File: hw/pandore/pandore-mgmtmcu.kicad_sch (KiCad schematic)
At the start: 40 parts, among them J17 GROVE, J18 GROVE, J25 DISPLAY, J26 RGBA, Q10 MOSFET_EN-N, Q8 MOSFET_EN-N, Q9 MOSFET_EN-N, U25 x4xxxx1G04

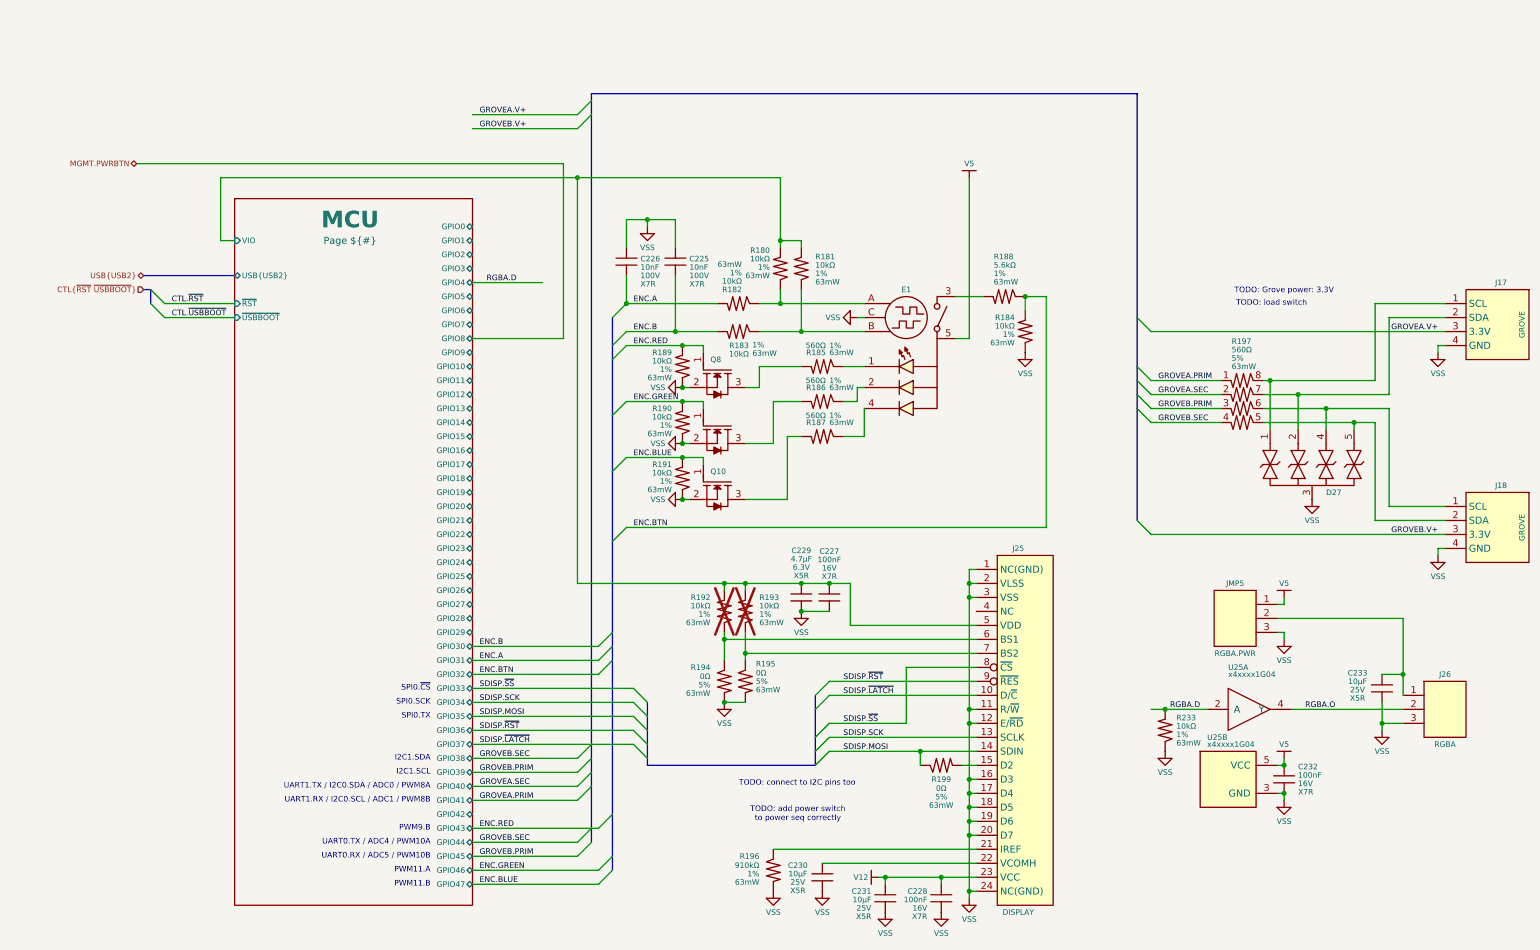
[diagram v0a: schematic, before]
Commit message: added expansion port and more ctl to rp2350s routing much progress
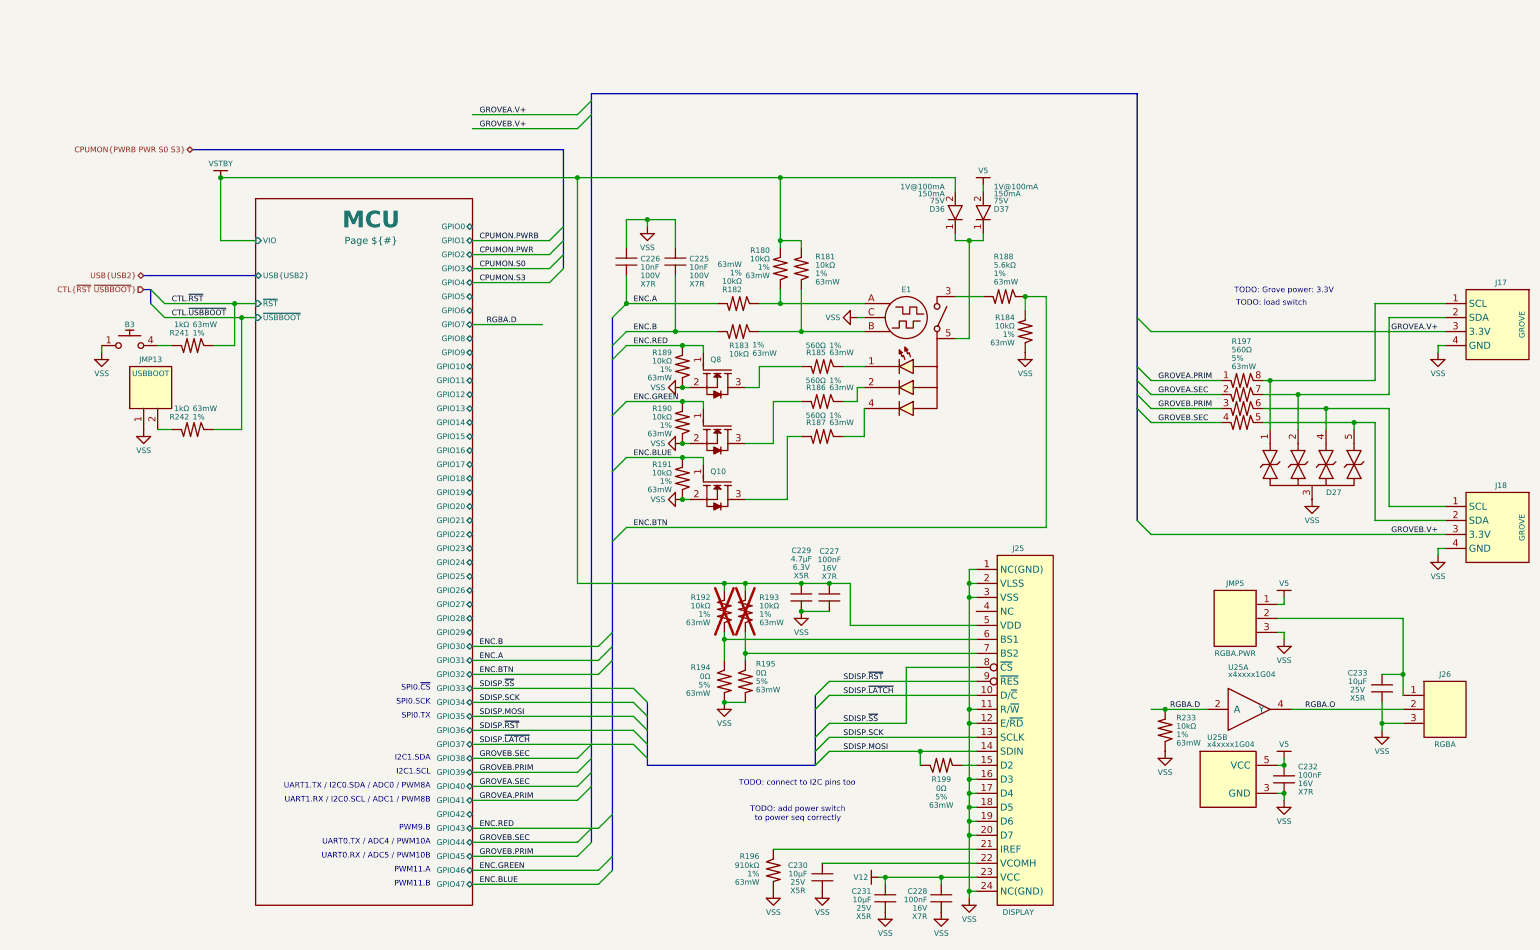
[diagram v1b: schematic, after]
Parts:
- added B3: mom_tact_no, reekilib_msw:tact_460X320X250, symbol reekilib_msw:mom_tact_no
- added D36, D37: ${Vr}, ${Io}, ${Vf}, reekilib_sod:sod-123, symbol reekilib_dio:diode
- added JMP13: USBBOOT, reekilib_con:HDR254P1X02-TH, symbol reekilib_con:hdr-1x2
- added R241, R242: ${Resistance}, ${Tolerance}, ${Power}, reekilib_res:RESC1005, symbol reekilib_res:res
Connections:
- net CTL.~{RST}: now also R241.2
- net CTL.~{USBBOOT}: now also R242.2
- net V5: now also D37.2 (A); no longer E1.5 (CM)
- net VSS: now also B3.1, B3.2, JMP13.1
- net MCU/VIO renamed VSTBY
- net VSTBY: now also D36.2 (A)
- new net: D36.1 (C), D37.1 (C), E1.5 (CM)
- new net: JMP13.2, R242.1
- new net: B3.3, B3.4, R241.1

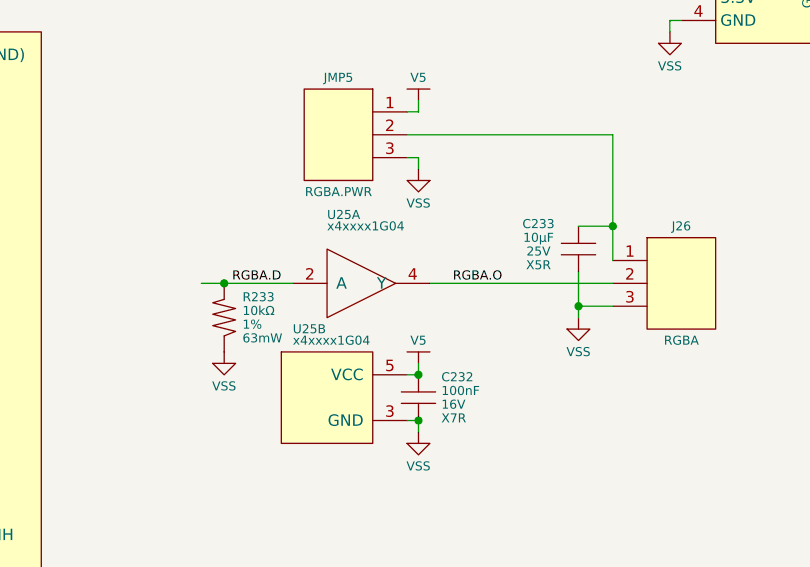
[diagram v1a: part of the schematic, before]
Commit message: more routing/placement done added 5v load switch 1A each added second fan circuit redone all diffpair routing following new stackup calc added all (?) missing connectors to unused pins
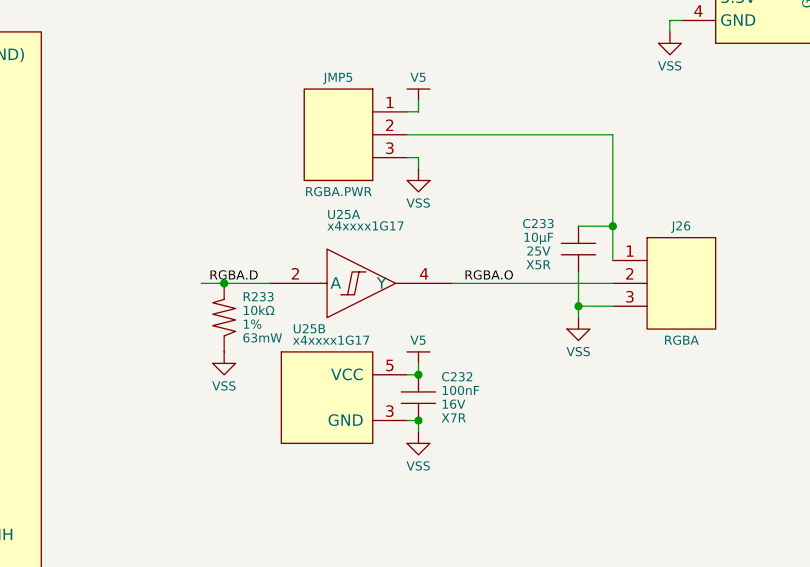
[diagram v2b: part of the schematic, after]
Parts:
- removed U25: x4xxxx1G04, reekilib_sot:SOT65P210X90-5, symbol reekilib_log:x4xxxx1G04
- added U25: x4xxxx1G17, reekilib_sot:SOT65P210X90-5, symbol reekilib_log:x4xxxx1G17
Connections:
- net RGBA.D: now also U25.2 (A)
- net RGBA.O: now also U25.4 (Y)
- net V5: now also U25.5 (VCC)
- net VSS: now also U25.3 (GND)

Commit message: last sprint almost done, most routing done
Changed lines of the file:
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@@
 	)
 	(label "CPUMON.S0"
-		(at 88.9 62.23 0)
+		(at 88.9 64.77 0)
 		(effects
 			(font
@@
 	)
 	(label "CPUMON.S3"
-		(at 88.9 64.77 0)
+		(at 88.9 62.23 0)
 		(effects
 			(font

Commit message: finished adding mpn,mfg to all parts, finished routing placement
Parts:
- added C291, C292: ${Capacitance}, ${Voltage}, ${Dielectric}, reekilib_cap:CAPC1005, symbol reekilib_cap:cap
- added PTC1, PTC2: PTC, megaxone_passive:FUSER1608, symbol megaxone_protection:PTC
- added R283: ${Resistance}, ${Tolerance}, ${Power}, reekilib_res:RESC1005, symbol reekilib_res:res
- added U37: BMI270, reekilib_qfn:QFN50P250X300-14, symbol reekilib_sns:BMI270
- added V12: 3d axis, reekilib_vrt:axis_cartesian_3d, symbol reekilib_vrt:virtual
- C225, C226: MFG (none) -> Murata; MPN (none) -> GCM188R72A103KA37D
- C227, C228, C232: MFG2 Samsung Electro-Mechanics -> (none); MFG3 Taiyo Yuden -> (none); MPN2 CL05B104KA5NNNC -> (none); MPN3 EMK105B7104KV-F -> (none); Voltage 16V -> 25V
- C230, C231, C233: MFG (none) -> Murata; MPN (none) -> GRM21BR61E106KA73K
- J26, JMP5: Link url-link -> (none); MFG MFG -> Adam Tech; MPN MPN -> PH1-03-UA
- JMP13: MFG (none) -> Adam Tech; MPN (none) -> PH1-02-UA
- R185, R186, R187: Link (none) -> https://yageogroup.com/products/Resistors/part/RC0402FR-075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; MFG (none) -> YAGEO; MPN (none) -> RC0402FR-07560RL
- R188: Link (none) -> https://yageogroup.com/products/Resistors/part/RC0402FR-075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; MFG (none) -> YAGEO; MPN (none) -> RC0402FR-075K6L
- R194, R195, R199: Link (none) -> https://yageogroup.com/products/Resistors/part/RC0402JR-070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; MFG (none) -> Yageo; MFG2 (none) -> Stackpole; MFG3 (none) -> Vishay Dale; MPN (none) -> RC0402JR-070RL; MPN2 (none) -> RMCF0402ZT0R00; MPN3 (none) -> CRCW04020000Z0ED
- R196: Link (none) -> https://yageogroup.com/products/Resistors/part/RC0402FR-079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; MFG (none) -> YAGEO; MPN (none) -> RC0402FR-07910KL
- R241, R242: Link (none) -> https://yageogroup.com/products/Resistors/part/RC0402FR-131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; MFG (none) -> YAGEO; MPN (none) -> RC0402FR-131KL
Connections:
- net GROVEA.V+: now also PTC1.2
- net GROVEB.V+: now also PTC2.2
- net VSS: now also C291.1, C292.1, U37.6 (GNDIO), U37.7 (GND)
- net VSTBY: now also C291.2, C292.2, PTC1.1, PTC2.1, R283.1, U37.5 (VDDIO), U37.8 (VDD)
- new net IMU.IRQ1: U37.4 (INT1)
- new net IMU.IRQ2: U37.9 (INT2)
- new net IMU.MISO: U37.1 (SDO)
- new net IMU.MOSI: U37.14 (SDI)
- new net IMU.SCK: U37.13 (SCK)
- new net IMU.~{SS}: R283.2, U37.12 (~{CS})
- no-connect marks 0 -> 4
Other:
- note removed: "TODO: Grove power: 3.3V"
